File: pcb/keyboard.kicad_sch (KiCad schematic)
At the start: 51 parts, among them J1 TRRS, SW11 Switch, SW12 Switch, SW13 Switch, SW14 Switch, SW15 Switch, SW16 Switch, SW17 Switch, SW18 Switch, SW19 Switch, SW21 Switch, SW22 Switch, SW23 Switch, SW24 Switch, SW25 Switch, SW26 Switch, SW27 Switch, SW28 Switch, SW29 Switch, SW31 Switch, SW32 Switch, SW33 Switch, SW34 Switch, SW35 Switch, SW36 Switch, SW37 Switch, SW38 Switch, SW39 Switch, SW41 Switch, SW42 Switch, SW43 Switch, SW44 Switch, SW45 Switch, SW46 Switch, SW47 Switch, SW48 Switch, SW49 Switch, U1 EliteC

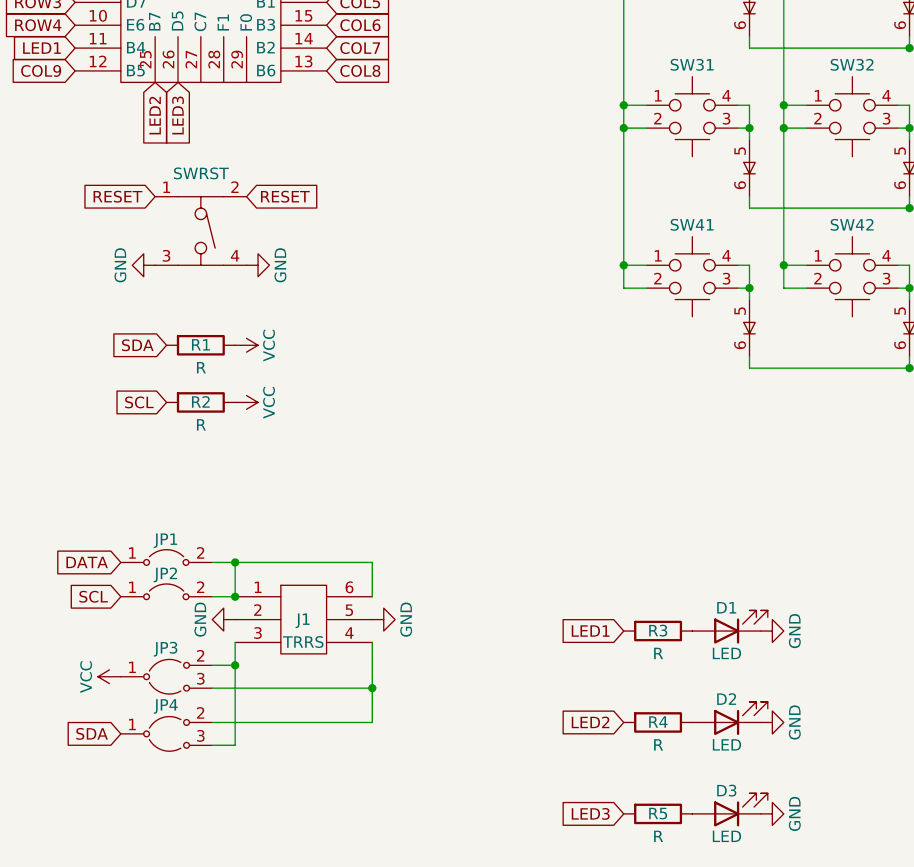
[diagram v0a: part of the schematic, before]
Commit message: add LED and fix footprints references and positioning
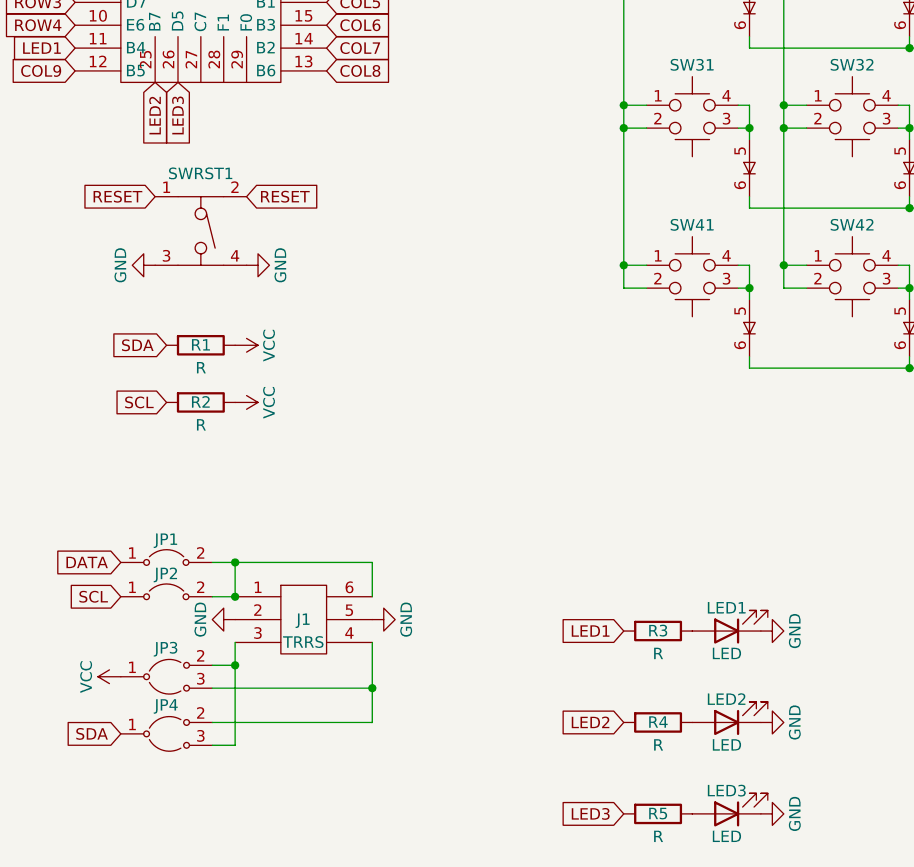
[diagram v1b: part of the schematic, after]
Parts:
- J1: footprint (none) -> Keyboard:PJ-320A
- JP1, JP2: footprint (none) -> Keyboard:Jumper
- JP3, JP4: value Jumper -> JumperSplit; footprint (none) -> Keyboard:JumperSplit
- LED1: renamed from D1; footprint (none) -> Keyboard:LED
- LED2: renamed from D2; footprint (none) -> Keyboard:LED
- LED3: renamed from D3; footprint (none) -> Keyboard:LED
- R1, R2, R3, R4, R5: footprint (none) -> Keyboard:SDR18
- SW11, SW12, SW13, SW14, SW15, SW16, SW17, SW18, SW19, SW21, SW22, SW23, SW24, SW25, SW26, SW27, SW28, SW29, SW31, SW32, SW33, SW34, SW35, SW36, SW37, SW38, SW39, SW41, SW42, SW43, SW44, SW45, SW46, SW47, SW48, SW49: footprint (none) -> Keyboard:Switch
- SWRST1: renamed from SWRST; footprint (none) -> Keyboard:PTS526
- U1: footprint (none) -> Keyboard:EliteC

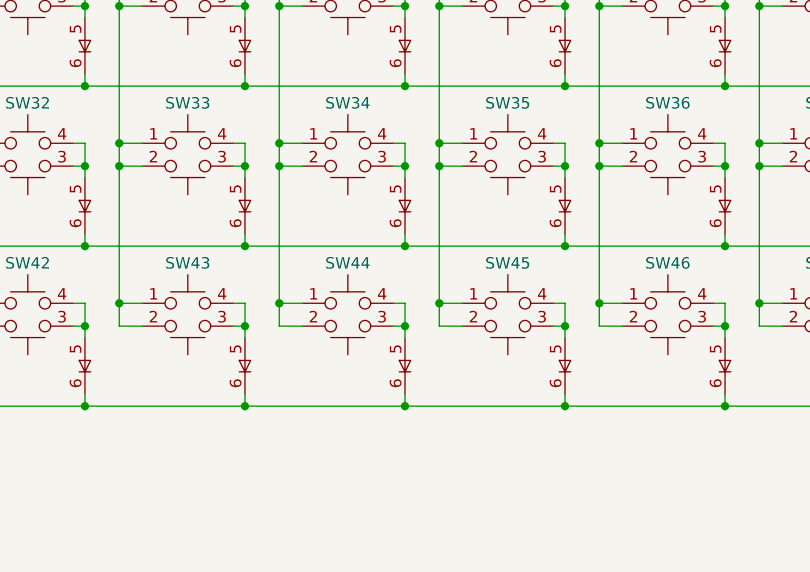
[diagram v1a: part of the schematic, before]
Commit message: remove excess switch in schematic
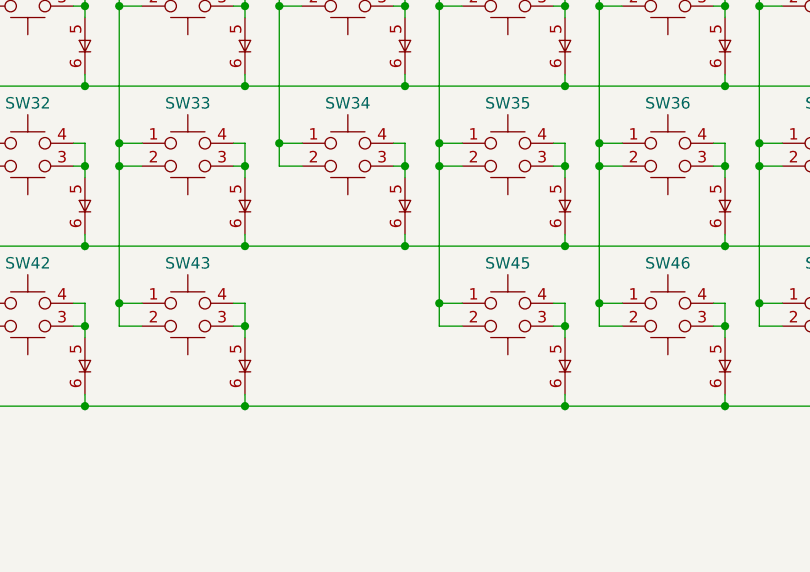
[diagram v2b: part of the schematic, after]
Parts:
- removed SW44: Switch, Keyboard:Switch, symbol Keyboard:Switch
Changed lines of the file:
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@@
   (junction (at 191.77 57.15) (diameter 0) (color 0 0 0 0)
   )
-  (junction (at 156.21 92.71) (diameter 0) (color 0 0 0 0)
-  )
   (junction (at 259.08 59.69) (diameter 0) (color 0 0 0 0)
   )
@@
   (junction (at 205.74 68.58) (diameter 0) (color 0 0 0 0)
   )
-  (junction (at 170.18 95.25) (diameter 0) (color 0 0 0 0)
-  )
   (junction (at 152.4 50.8) (diameter 0) (color 0 0 0 0)
   )
@@
   (junction (at 173.99 74.93) (diameter 0) (color 0 0 0 0)
   )
-  (junction (at 170.18 104.14) (diameter 0) (color 0 0 0 0)
-  )
   (junction (at 241.3 77.47) (diameter 0) (color 0 0 0 0)
   )
@@
   )
   (junction (at 259.08 41.91) (diameter 0) (color 0 0 0 0)
-  )
-  (junction (at 156.21 77.47) (diameter 0) (color 0 0 0 0)
   )
   (junction (at 170.18 68.58) (diameter 0) (color 0 0 0 0)
@@
     (stroke (width 0) (type default))
   )
-  (wire (pts (xy 187.96 104.14) (xy 170.18 104.14))
+  (wire (pts (xy 152.4 104.14) (xy 187.96 104.14))
     (stroke (width 0) (type default))
   )
@@
     (stroke (width 0) (type default))
   )
-  (wire (pts (xy 170.18 92.71) (xy 170.18 95.25))
-    (stroke (width 0) (type default))
-  )
   (wire (pts (xy 205.74 57.15) (xy 205.74 59.69))
     (stroke (width 0) (type default))
@@
     (stroke (width 0) (type default))
   )
-  (wire (pts (xy 170.18 104.14) (xy 152.4 104.14))
-    (stroke (width 0) (type default))
-  )
   (wire (pts (xy 102.87 41.91) (xy 102.87 57.15))
     (stroke (width 0) (type default))
@@
     (stroke (width 0) (type default))
   )
-  (wire (pts (xy 156.21 92.71) (xy 156.21 95.25))
-    (stroke (width 0) (type default))
-  )
   (wire (pts (xy 120.65 77.47) (xy 120.65 92.71))
     (stroke (width 0) (type default))
@@
     (stroke (width 0) (type default))
   )
-  (wire (pts (xy 158.75 95.25) (xy 156.21 95.25))
-    (stroke (width 0) (type default))
-  )
   (wire (pts (xy 134.62 74.93) (xy 134.62 77.47))
     (stroke (width 0) (type default))
@@
     (stroke (width 0) (type default))
   )
-  (wire (pts (xy 168.91 95.25) (xy 170.18 95.25))
-    (stroke (width 0) (type default))
-  )
   (wire (pts (xy 170.18 74.93) (xy 170.18 77.47))
     (stroke (width 0) (type default))
@@
     (stroke (width 0) (type default))
   )
-  (wire (pts (xy 170.18 102.87) (xy 170.18 104.14))
-    (stroke (width 0) (type default))
-  )
   (wire (pts (xy 120.65 39.37) (xy 120.65 41.91))
     (stroke (width 0) (type default))
@@
     (stroke (width 0) (type default))
   )
-  (wire (pts (xy 156.21 77.47) (xy 156.21 92.71))
-    (stroke (width 0) (type default))
-  )
   (wire (pts (xy 240.03 95.25) (xy 241.3 95.25))
     (stroke (width 0) (type default))
@@
     (stroke (width 0) (type default))
   )
-  (wire (pts (xy 170.18 95.25) (xy 170.18 96.52))
-    (stroke (width 0) (type default))
-  )
   (wire (pts (xy 134.62 57.15) (xy 134.62 59.69))
     (stroke (width 0) (type default))
@@
     (stroke (width 0) (type default))
   )
-  (wire (pts (xy 156.21 92.71) (xy 158.75 92.71))
-    (stroke (width 0) (type default))
-  )
   (wire (pts (xy 59.69 125.73) (xy 74.93 125.73))
     (stroke (width 0) (type default))
@@
   )
   (wire (pts (xy 138.43 92.71) (xy 140.97 92.71))
-    (stroke (width 0) (type default))
-  )
-  (wire (pts (xy 168.91 92.71) (xy 170.18 92.71))
     (stroke (width 0) (type default))
   )
@@
         )
       )
-    )
-  )
-  (symbol (lib_id "Keyboard:Switch") (at 163.83 93.98 0) (unit 1)
-    (in_bom yes) (on_board yes) (dnp no) (fields_autoplaced)
-    (property "Reference" "SW44" (at 163.83 88.265 0) (do_not_autoplace)
-      (effects (font (size 1.27 1.27)))
-    )
-    (property "Value" "Switch" (at 163.83 99.695 0) (do_not_autoplace)
-      (effects (font (size 1.27 1.27)) hide)
-    )
-    (property "Footprint" "Keyboard:Switch" (at 163.83 93.98 0)
-      (effects (font (size 1.27 1.27)) hide)
-    )
-    (property "Datasheet" "" (at 163.83 93.98 0)
-      (effects (font (size 1.27 1.27)) hide)
-    )
-    (pin "1")
-    (pin "2")
-    (pin "3")
-    (pin "4")
-    (pin "5")
-    (pin "6")
-    (instances
-      (project "keyboard"
-        (path "/7807834d-3d77-4d25-b9d8-d933072c7b84"
-          (reference "SW44") (unit 1)
-        )
-      )

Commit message: set switch number to silkscreen
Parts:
- SW11: value Switch -> 1
- SW12: value Switch -> 2
- SW13: value Switch -> 3
- SW14: value Switch -> 4
- SW15: value Switch -> 5
- SW16: value Switch -> 6
- SW17: value Switch -> 7
- SW18: value Switch -> 8
- SW19: value Switch -> 9
- SW21: value Switch -> 11
- SW22: value Switch -> 12
- SW23: value Switch -> 13
- SW24: value Switch -> 14
- SW25: value Switch -> 15
- SW26: value Switch -> 16
- SW27: value Switch -> 17
- SW28: value Switch -> 18
- SW29: value Switch -> 19
- SW31: value Switch -> 21
- SW32: value Switch -> 22
- SW33: value Switch -> 23
- SW34: value Switch -> 24
- SW35: value Switch -> 25
- SW36: value Switch -> 26
- SW37: value Switch -> 27
- SW38: value Switch -> 28
- SW39: value Switch -> 29
- SW41: value Switch -> 31
- SW42: value Switch -> 32
- SW43: value Switch -> 33
- SW45: value Switch -> 35
- SW46: value Switch -> 36
- SW47: value Switch -> 37
- SW48: value Switch -> 38
- SW49: value Switch -> 39
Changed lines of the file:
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@@
       (effects (font (size 1.27 1.27)))
     )
-    (property "Value" "Switch" (at 128.27 46.355 0) (do_not_autoplace)
+    (property "Value" "2" (at 128.27 46.355 0) (do_not_autoplace)
       (effects (font (size 1.27 1.27)) hide)
     )
@@
       (effects (font (size 1.27 1.27)))
     )
-    (property "Value" "Switch" (at 163.83 81.915 0) (do_not_autoplace)
+    (property "Value" "24" (at 163.83 81.915 0) (do_not_autoplace)
       (effects (font (size 1.27 1.27)) hide)
     )
@@
       (effects (font (size 1.27 1.27)))
     )
-    (property "Value" "Switch" (at 217.17 81.915 0) (do_not_autoplace)
+    (property "Value" "27" (at 217.17 81.915 0) (do_not_autoplace)
       (effects (font (size 1.27 1.27)) hide)
     )
@@
       (effects (font (size 1.27 1.27)))
     )
-    (property "Value" "Switch" (at 146.05 99.695 0) (do_not_autoplace)
+    (property "Value" "33" (at 146.05 99.695 0) (do_not_autoplace)
       (effects (font (size 1.27 1.27)) hide)
     )
@@
       (effects (font (size 1.27 1.27)))
     )
-    (property "Value" "Switch" (at 110.49 99.695 0) (do_not_autoplace)
+    (property "Value" "31" (at 110.49 99.695 0) (do_not_autoplace)
       (effects (font (size 1.27 1.27)) hide)
     )
@@
       (effects (font (size 1.27 1.27)))
     )
-    (property "Value" "Switch" (at 217.17 46.355 0) (do_not_autoplace)
+    (property "Value" "7" (at 217.17 46.355 0) (do_not_autoplace)
       (effects (font (size 1.27 1.27)) hide)
     )
@@
       (effects (font (size 1.27 1.27)))
     )
-    (property "Value" "Switch" (at 199.39 81.915 0) (do_not_autoplace)
+    (property "Value" "26" (at 199.39 81.915 0) (do_not_autoplace)
       (effects (font (size 1.27 1.27)) hide)
     )
@@
       (effects (font (size 1.27 1.27)))
     )
-    (property "Value" "Switch" (at 217.17 64.135 0) (do_not_autoplace)
+    (property "Value" "17" (at 217.17 64.135 0) (do_not_autoplace)
       (effects (font (size 1.27 1.27)) hide)
     )
@@
       (effects (font (size 1.27 1.27)))
     )
-    (property "Value" "Switch" (at 252.73 64.135 0) (do_not_autoplace)
+    (property "Value" "19" (at 252.73 64.135 0) (do_not_autoplace)
       (effects (font (size 1.27 1.27)) hide)
     )
@@
       (effects (font (size 1.27 1.27)))
     )
-    (property "Value" "Switch" (at 163.83 46.355 0) (do_not_autoplace)
+    (property "Value" "4" (at 163.83 46.355 0) (do_not_autoplace)
       (effects (font (size 1.27 1.27)) hide)
     )
@@
       (effects (font (size 1.27 1.27)))
     )
-    (property "Value" "Switch" (at 128.27 64.135 0) (do_not_autoplace)
+    (property "Value" "12" (at 128.27 64.135 0) (do_not_autoplace)
       (effects (font (size 1.27 1.27)) hide)
     )
@@
       (effects (font (size 1.27 1.27)))
     )
-    (property "Value" "Switch" (at 146.05 81.915 0) (do_not_autoplace)
+    (property "Value" "23" (at 146.05 81.915 0) (do_not_autoplace)
       (effects (font (size 1.27 1.27)) hide)
     )
@@
       (effects (font (size 1.27 1.27)))
     )
-    (property "Value" "Switch" (at 252.73 99.695 0) (do_not_autoplace)
+    (property "Value" "39" (at 252.73 99.695 0) (do_not_autoplace)
       (effects (font (size 1.27 1.27)) hide)
     )
@@
       (effects (font (size 1.27 1.27)))
     )
-    (property "Value" "Switch" (at 110.49 46.355 0) (do_not_autoplace)
+    (property "Value" "1" (at 110.49 46.355 0) (do_not_autoplace)
       (effects (font (size 1.27 1.27)) hide)
     )
@@
       (effects (font (size 1.27 1.27)))
     )
-    (property "Value" "Switch" (at 252.73 81.915 0) (do_not_autoplace)
+    (property "Value" "29" (at 252.73 81.915 0) (do_not_autoplace)
       (effects (font (size 1.27 1.27)) hide)
     )
@@
       (effects (font (size 1.27 1.27)))
     )
-    (property "Value" "Switch" (at 199.39 64.135 0) (do_not_autoplace)
+    (property "Value" "16" (at 199.39 64.135 0) (do_not_autoplace)
       (effects (font (size 1.27 1.27)) hide)
     )
@@
       (effects (font (size 1.27 1.27)))
     )
-    (property "Value" "Switch" (at 181.61 99.695 0) (do_not_autoplace)
+    (property "Value" "35" (at 181.61 99.695 0) (do_not_autoplace)
       (effects (font (size 1.27 1.27)) hide)
     )
@@
       (effects (font (size 1.27 1.27)))
     )
-    (property "Value" "Switch" (at 181.61 64.135 0) (do_not_autoplace)
+    (property "Value" "15" (at 181.61 64.135 0) (do_not_autoplace)
       (effects (font (size 1.27 1.27)) hide)
     )
@@
       (effects (font (size 1.27 1.27)))
     )
-    (property "Value" "Switch" (at 110.49 64.135 0) (do_not_autoplace)
+    (property "Value" "11" (at 110.49 64.135 0) (do_not_autoplace)
       (effects (font (size 1.27 1.27)) hide)
     )
@@
       (effects (font (size 1.27 1.27)))
     )
-    (property "Value" "Switch" (at 128.27 81.915 0) (do_not_autoplace)
+    (property "Value" "22" (at 128.27 81.915 0) (do_not_autoplace)
       (effects (font (size 1.27 1.27)) hide)
     )
@@
       (effects (font (size 1.27 1.27)))
     )
-    (property "Value" "Switch" (at 181.61 81.915 0) (do_not_autoplace)
+    (property "Value" "25" (at 181.61 81.915 0) (do_not_autoplace)
       (effects (font (size 1.27 1.27)) hide)
     )
@@
       (effects (font (size 1.27 1.27)))
     )
-    (property "Value" "Switch" (at 146.05 64.135 0) (do_not_autoplace)
+    (property "Value" "13" (at 146.05 64.135 0) (do_not_autoplace)
       (effects (font (size 1.27 1.27)) hide)
     )
@@
       (effects (font (size 1.27 1.27)))
     )
-    (property "Value" "Switch" (at 110.49 81.915 0) (do_not_autoplace)
+    (property "Value" "21" (at 110.49 81.915 0) (do_not_autoplace)
       (effects (font (size 1.27 1.27)) hide)
     )
@@
       (effects (font (size 1.27 1.27)))
     )
-    (property "Value" "Switch" (at 199.39 46.355 0) (do_not_autoplace)
+    (property "Value" "6" (at 199.39 46.355 0) (do_not_autoplace)
       (effects (font (size 1.27 1.27)) hide)
     )
@@
       (effects (font (size 1.27 1.27)))
     )
-    (property "Value" "Switch" (at 199.39 99.695 0) (do_not_autoplace)
+    (property "Value" "36" (at 199.39 99.695 0) (do_not_autoplace)
       (effects (font (size 1.27 1.27)) hide)
     )
@@
       (effects (font (size 1.27 1.27)))
     )
-    (property "Value" "Switch" (at 234.95 64.135 0) (do_not_autoplace)
+    (property "Value" "18" (at 234.95 64.135 0) (do_not_autoplace)
       (effects (font (size 1.27 1.27)) hide)
     )
@@
       (effects (font (size 1.27 1.27)))
     )
-    (property "Value" "Switch" (at 146.05 46.355 0) (do_not_autoplace)
+    (property "Value" "3" (at 146.05 46.355 0) (do_not_autoplace)
       (effects (font (size 1.27 1.27)) hide)
     )
@@
       (effects (font (size 1.27 1.27)))
     )
-    (property "Value" "Switch" (at 234.95 81.915 0) (do_not_autoplace)
+    (property "Value" "28" (at 234.95 81.915 0) (do_not_autoplace)
       (effects (font (size 1.27 1.27)) hide)
     )
@@
       (effects (font (size 1.27 1.27)))
     )
-    (property "Value" "Switch" (at 234.95 99.695 0) (do_not_autoplace)
+    (property "Value" "38" (at 234.95 99.695 0) (do_not_autoplace)
       (effects (font (size 1.27 1.27)) hide)
     )
@@
       (effects (font (size 1.27 1.27)))
     )
-    (property "Value" "Switch" (at 252.73 46.355 0) (do_not_autoplace)
+    (property "Value" "9" (at 252.73 46.355 0) (do_not_autoplace)
       (effects (font (size 1.27 1.27)) hide)
     )
@@
       (effects (font (size 1.27 1.27)))
     )
-    (property "Value" "Switch" (at 163.83 64.135 0) (do_not_autoplace)
+    (property "Value" "14" (at 163.83 64.135 0) (do_not_autoplace)
       (effects (font (size 1.27 1.27)) hide)
     )
@@
       (effects (font (size 1.27 1.27)))
     )
-    (property "Value" "Switch" (at 217.17 99.695 0) (do_not_autoplace)
+    (property "Value" "37" (at 217.17 99.695 0) (do_not_autoplace)
       (effects (font (size 1.27 1.27)) hide)
     )
@@
       (effects (font (size 1.27 1.27)))
     )
-    (property "Value" "Switch" (at 234.95 46.355 0) (do_not_autoplace)
+    (property "Value" "8" (at 234.95 46.355 0) (do_not_autoplace)
       (effects (font (size 1.27 1.27)) hide)
     )
@@
       (effects (font (size 1.27 1.27)))
     )
-    (property "Value" "Switch" (at 181.61 46.355 0) (do_not_autoplace)
+    (property "Value" "5" (at 181.61 46.355 0) (do_not_autoplace)
       (effects (font (size 1.27 1.27)) hide)
     )
@@
       (effects (font (size 1.27 1.27)))
     )
-    (property "Value" "Switch" (at 128.27 99.695 0) (do_not_autoplace)
-      (effects (font (size 1.27 1.27)) hide)
-    )
+    (property "Value" "32" (at 128.27 99.695 0) (do_not_autoplace)
+      (effects (font (size 1.27 1.27)) hide)
+    )

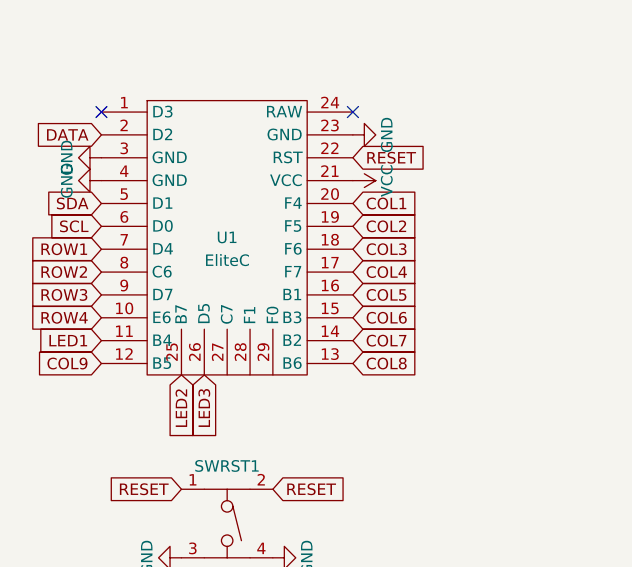
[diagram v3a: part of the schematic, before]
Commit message: add lots of traces and remove solder mask from jumpers
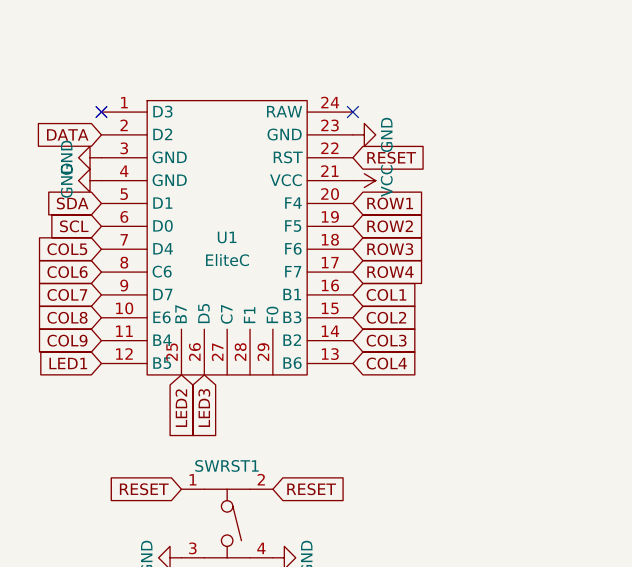
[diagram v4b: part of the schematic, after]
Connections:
- net COL1: now also U1.16 (B1); no longer U1.20 (F4)
- net COL2: now also U1.15 (B3); no longer U1.19 (F5)
- net COL3: now also U1.14 (B2); no longer U1.18 (F6)
- net COL4: now also U1.13 (B6); no longer U1.17 (F7)
- net COL5: now also U1.7 (D4); no longer U1.16 (B1)
- net COL6: now also U1.8 (C6); no longer U1.15 (B3)
- net COL7: now also U1.9 (D7); no longer U1.14 (B2)
- net COL8: now also U1.10 (E6); no longer U1.13 (B6)
- net COL9: now also U1.11 (B4); no longer U1.12 (B5)
- net LED1: now also U1.12 (B5); no longer U1.11 (B4)
- net ROW1: now also U1.20 (F4); no longer U1.7 (D4)
- net ROW2: now also U1.19 (F5); no longer U1.8 (C6)
- net ROW3: now also U1.18 (F6); no longer U1.9 (D7)
- net ROW4: now also U1.17 (F7); no longer U1.10 (E6)
